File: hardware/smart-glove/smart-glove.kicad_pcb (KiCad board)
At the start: 2 copper layers, 60 x 45 mm, 33 parts, among them J1 USB-C, J2 FLEX, J3 LiPo, J4 UART, SW1 BOOT, SW2 EN, U1 ESP32-WROOM-32E, U2 TP4056, U3 AMS1117-3.3, U4 MPU-6050

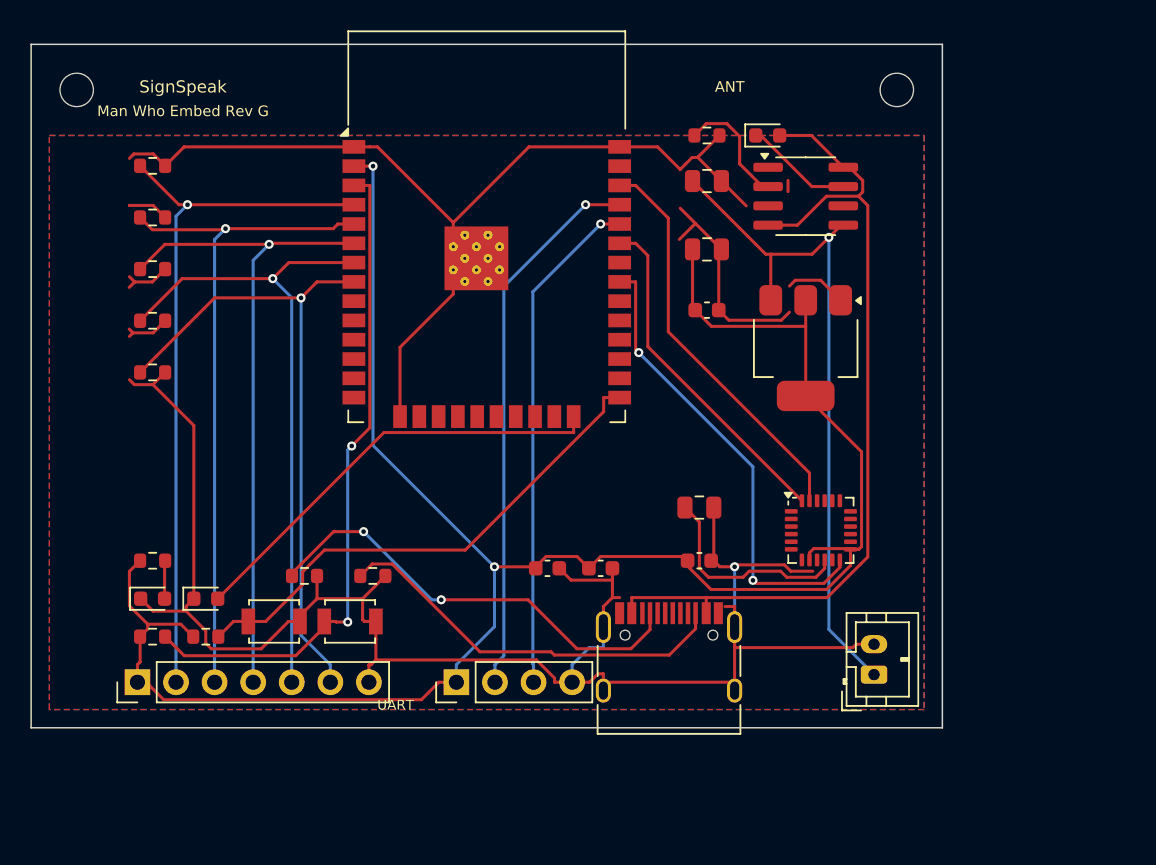
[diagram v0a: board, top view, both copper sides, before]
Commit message: Rev H: USB-C CH340, LiPo protect, firmware, compliance package
Resolves production gaps: onboard USB serial (CH340), DW01+FS8205
battery protection, RF mounting guide, LCSC BOM, assembly notes,
compliance path docs, and SignSpeak Arduino firmware with serial CSV.

Co-authored-by: ADIL ZAHOOR  <adilzahoor2812@users.noreply.github.com>
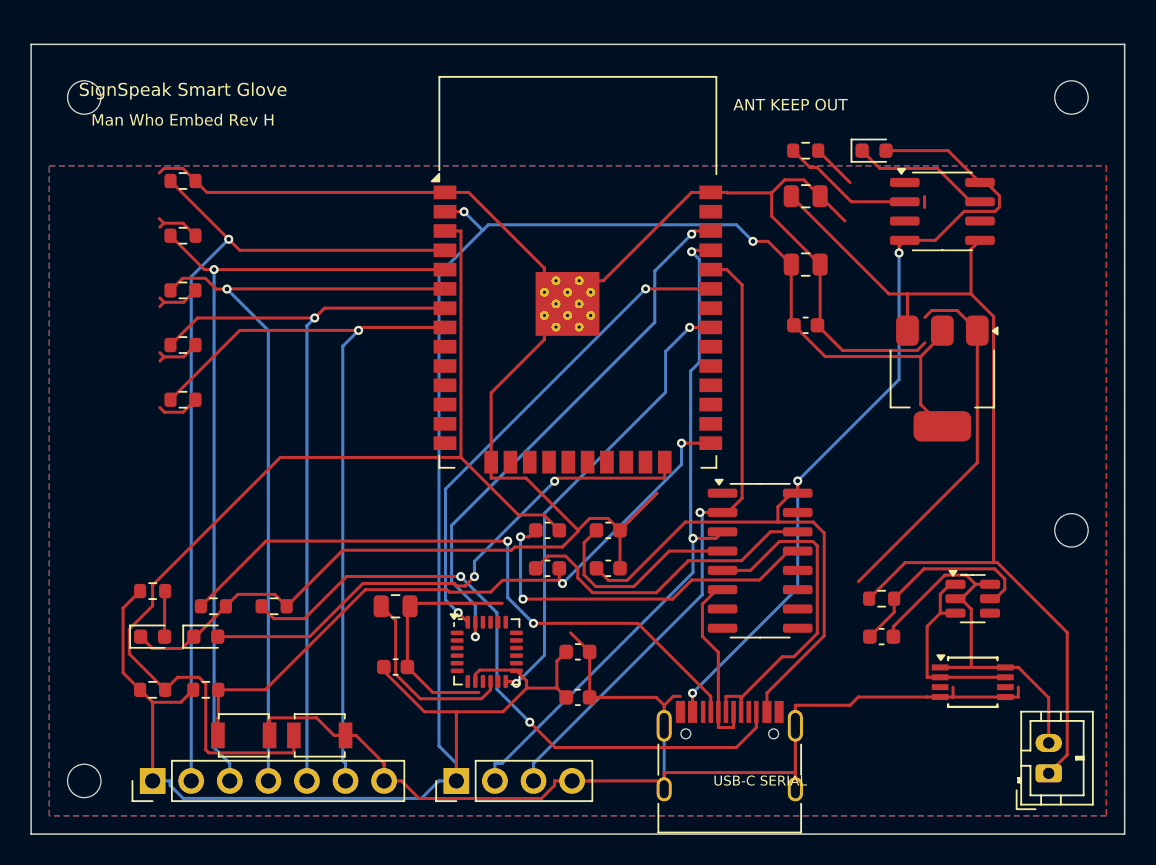
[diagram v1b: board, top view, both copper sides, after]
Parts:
- added C11: 100nF, C_0603_1608Metric, F.Cu at (34.0, 32.0)
- added C12: 100nF, C_0603_1608Metric, F.Cu at (34.0, 34.5)
- added C13: 100nF, C_0603_1608Metric, F.Cu at (38.0, 32.0)
- added C14: 100nF, C_0603_1608Metric, F.Cu at (38.0, 34.5)
- added C15: 100nF, C_0603_1608Metric, F.Cu at (56.0, 39.0)
- added H3: M2, MountingHole_2.2mm_M2, F.Cu at (3.50, 48.5)
- added H4: M2, MountingHole_2.2mm_M2, F.Cu at (68.5, 32.0)
- added R12: 1k, R_0603_1608Metric, F.Cu at (56.0, 36.5)
- added U5: CH340C, SOIC-16_3.9x9.9mm_P1.27mm, F.Cu at (48.0, 34.0)
- added U6: DW01A, SOT-23-6, F.Cu at (62.0, 36.5)
- added U7: FS8205A, TSSOP-8_3x3mm_P0.65mm, F.Cu at (62.0, 42.0)
- moved U4 23.4 mm to (30.0, 40.0)
- moved C9 21.2 mm to (24.0, 41.0)
- moved C10 21.0 mm to (24.0, 37.0)
- moved J3 13.2 mm to (67.0, 48.0)
- moved H2 11.5 mm to (68.5, 3.50)
- moved U3 9.22 mm to (60.0, 22.0)
- moved U2 9.06 mm to (60.0, 11.0)
- moved C2 8.63 mm to (36.0, 43.0)
- moved SW1 7.76 mm to (14.0, 45.5)
- moved SW2 7.76 mm to (19.0, 45.5)
- moved J1 7.63 mm to (46.0, 48.0)
- moved D2 7.07 mm to (55.5, 7.00)
- moved R7 6.80 mm to (16.0, 37.0)
- moved U1 6.71 mm to (36.0, 18.0)
- moved C5 6.58 mm to (51.0, 10.0)
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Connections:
- J1 pad A6: (no net) -> USB_DP
- J1 pad A7: (no net) -> USB_DM
- J1 pad B6: (no net) -> USB_DP
- J1 pad B7: (no net) -> USB_DM
- J3 pad 2: GND -> BAT_N
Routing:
- net GND: track 222.3 -> 278.5 mm, vias 1 -> 0
- net +5V: track 57.3 -> 87.5 mm, vias 0 -> 3
- net EN: track 44.3 -> 71.3 mm, vias 2 -> 0
- net BAT_N: track 0.00 -> 26.3 mm
- net DTR: track 0.00 -> 24.7 mm, vias 0 -> 2
- net USB_DP: track 0.00 -> 22.7 mm
- net RTS: track 0.00 -> 20.6 mm
- net +BAT: track 45.8 -> 64.7 mm, vias 1 -> 0
- net CC2: track 26.6 -> 43.3 mm, vias 0 -> 2
- net CH340_3V3: track 0.00 -> 13.7 mm
- net DW01_VCC: track 0.00 -> 13.4 mm
- net GATE_P: track 0.00 -> 13.3 mm
- net CC1: track 29.7 -> 42.8 mm
- net USB_DM: track 0.00 -> 12.3 mm
- net 3V3: track 135.1 -> 147.3 mm
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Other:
- board size 60 x 45 mm -> 72 x 52 mm
- board text added: "ANT KEEP OUT"
- board text added: "Man Who Embed Rev H"
- board text added: "SignSpeak Smart Glove"
- board text added: "USB-C SERIAL"
- board text removed: "ANT"
- board text removed: "Man Who Embed Rev G"
- board text removed: "SignSpeak"
- board text removed: "UART"
